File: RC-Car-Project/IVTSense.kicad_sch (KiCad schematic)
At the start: 12 parts, among them U7 INA229AQDGSRQ1, U8 ADC082S021CIMM/NOPB

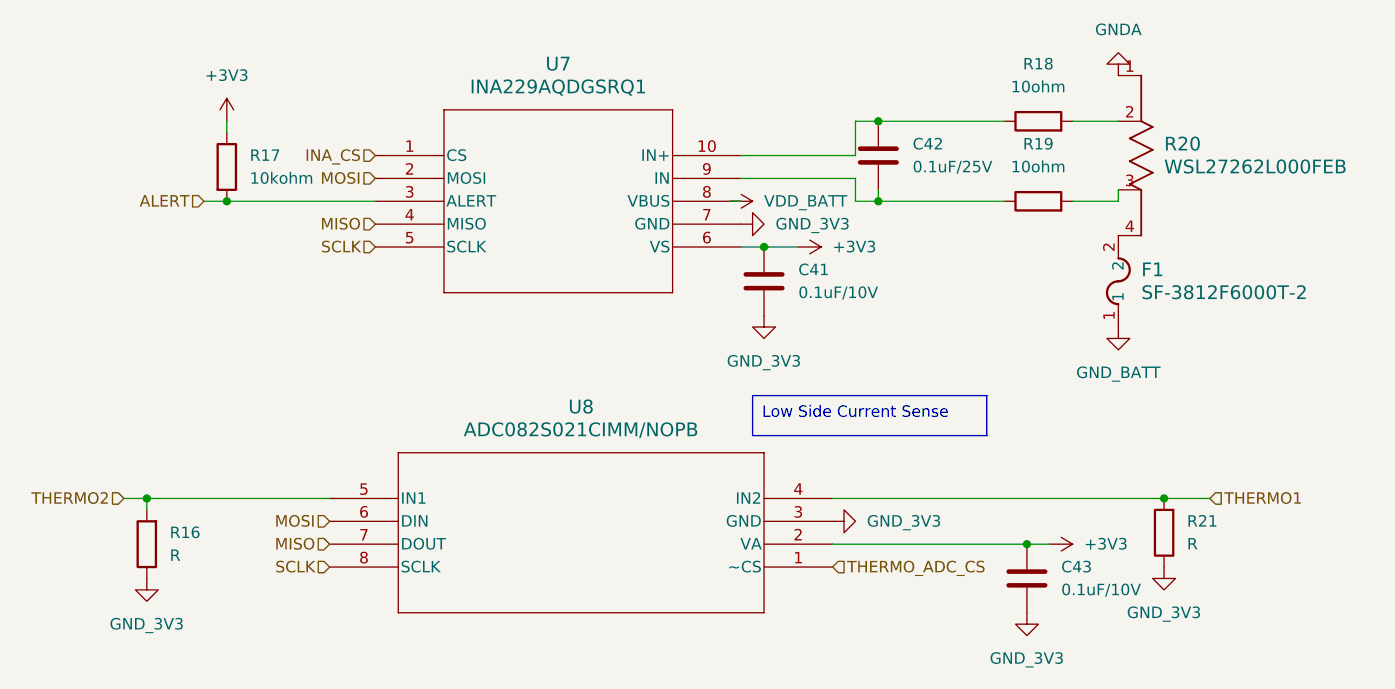
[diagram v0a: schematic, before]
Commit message: change footprint of cap some part num added
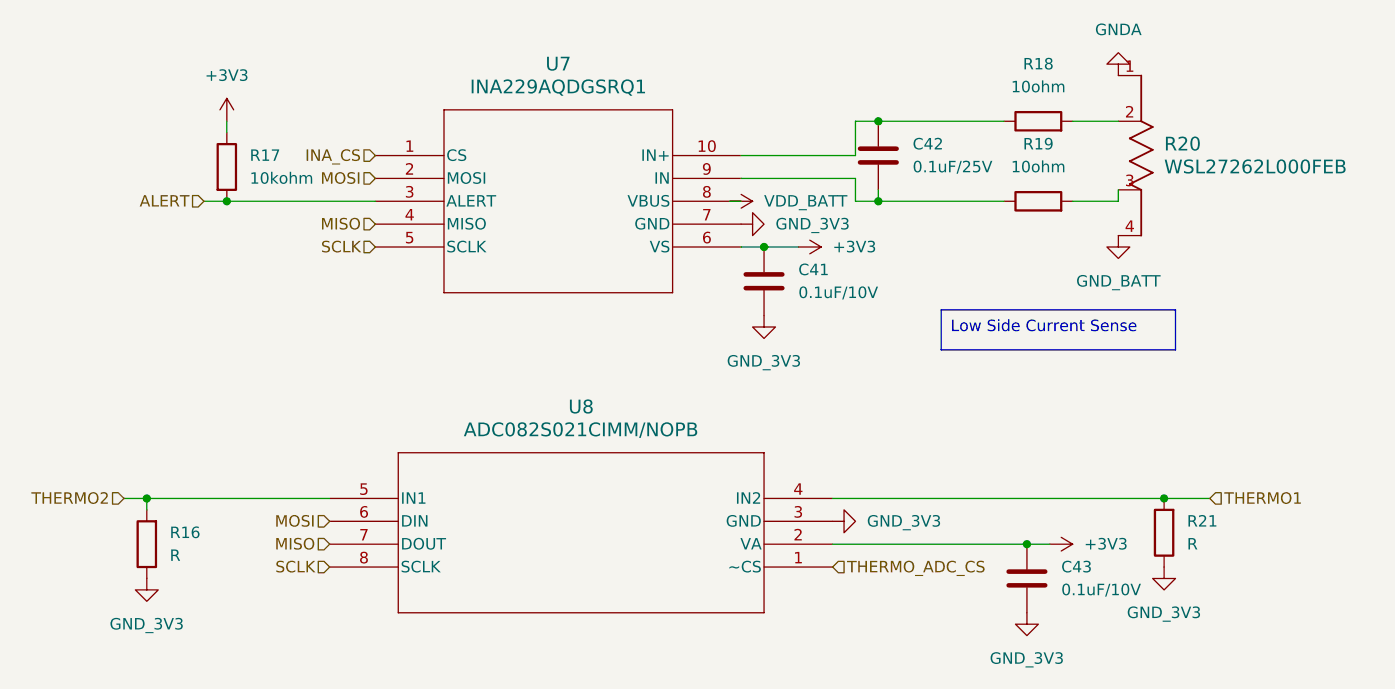
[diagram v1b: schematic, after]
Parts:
- removed F1: SF-3812F6000T-2, FUS_SF-3812F_BRN, symbol SF-3812F6000T-2:SF-3812F6000T-2
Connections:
- net GND_BATT: now also R20.4
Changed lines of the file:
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@@
 	(text_box "Low Side Current Sense\n"
 		(exclude_from_sim no)
-		(at 154.94 113.03 0)
+		(at 175.895 103.505 0)
 		(size 26.035 4.445)
 		(stroke
@@
 	)
 	(symbol
-		(lib_id "SF-3812F6000T-2:SF-3812F6000T-2")
-		(at 195.58 105.41 90)
-		(unit 1)
-		(exclude_from_sim no)
-		(in_bom yes)
-		(on_board yes)
-		(dnp no)
-		(fields_autoplaced yes)
-		(property "Reference" "F1"
-			(at 198.12 99.0599 90)
-			(effects
-				(font
-					(size 1.524 1.524)
-				)
-				(justify right)
-			)
-		)
-		(property "Value" "SF-3812F6000T-2"
-			(at 198.12 101.5999 90)
-			(effects
-				(font
-					(size 1.524 1.524)
-				)
-				(justify right)
-			)
-		)
-		(property "Footprint" "FUS_SF-3812F_BRN"
-			(at 195.58 105.41 0)
-			(effects
-				(font
-					(size 1.27 1.27)
-					(italic yes)
-				)
-				(hide yes)
-			)
-		)
-		(property "Datasheet" "SF-3812F6000T-2"
-			(at 195.58 105.41 0)
-			(effects
-				(font
-					(size 1.27 1.27)
-					(italic yes)
-				)
-				(hide yes)
-			)
-		)
-		(property "Description" ""
-			(at 195.58 105.41 0)
-			(effects
-				(font
-					(size 1.27 1.27)
-				)
-				(hide yes)
-			)
-		)
-		(pin "2"
-		)
-		(pin "1"
-		)
-		(instances
-			(project "RC-Car-Project"
-				(path "/ba870fd1-751d-4755-8e1a-1ea86ca9e2f6/9035ce50-cc35-47ce-85b3-06db8b07dac9"
-					(reference "F1")
-					(unit 1)
-				)
-			)
-		)
-	)
-	(symbol
 		(lib_id "Device:R")
 		(at 87.63 129.54 180)
@@
 			)
 		)
+		(property "MANUF_PN" ""
+			(at 87.63 129.54 0)
+			(effects
+				(font
+					(size 1.27 1.27)
+				)
+				(hide yes)
+			)
+		)
 		(pin "1"
 		)
@@
 			)
 		)
+		(property "MANUF_PN" ""
+			(at 195.58 80.01 0)
+			(effects
+				(font
+					(size 1.27 1.27)
+				)
+				(hide yes)
+			)
+		)
 		(pin "2"
 		)
@@
 			)
 		)
+		(property "MANUF_PN" ""
+			(at 186.69 91.44 0)
+			(effects
+				(font
+					(size 1.27 1.27)
+				)
+				(hide yes)
+			)
+		)
 		(pin "1"
 		)
@@
 			)
 		)
+		(property "MANUF_PN" ""
+			(at 185.42 133.35 0)
+			(effects
+				(font
+					(size 1.27 1.27)
+				)
+				(hide yes)
+			)
+		)
 		(pin "2"
 		)
@@
 			)
 		)
+		(property "MANUF_PN" ""
+			(at 200.66 128.27 0)
+			(effects
+				(font
+					(size 1.27 1.27)
+				)
+				(hide yes)
+			)
+		)
 		(pin "1"
 		)
@@
 			)
 		)
+		(property "MANUF_PN" ""
+			(at 168.91 86.36 0)
+			(effects
+				(font
+					(size 1.27 1.27)
+				)
+				(hide yes)
+			)
+		)
 		(pin "2"
 		)
@@
 	(symbol
 		(lib_id "power:GND")
-		(at 195.58 105.41 0)
+		(at 195.58 95.25 0)
 		(unit 1)
 		(exclude_from_sim no)
@@
 		(fields_autoplaced yes)
 		(property "Reference" "#PWR097"
-			(at 195.58 111.76 0)
+			(at 195.58 101.6 0)
 			(effects
 				(font
@@
 		)
 		(property "Value" "GND_BATT"
-			(at 195.58 110.49 0)
+			(at 195.58 100.33 0)
 			(effects
 				(font
@@
 		)
 		(property "Footprint" ""
-			(at 195.58 105.41 0)
+			(at 195.58 95.25 0)
 			(effects
 				(font
@@
 		)
 		(property "Datasheet" ""
-			(at 195.58 105.41 0)
+			(at 195.58 95.25 0)
 			(effects
 				(font
@@
 		)
 		(property "Description" "Power symbol creates a global label with name \"GND\" , ground"
-			(at 195.58 105.41 0)
+			(at 195.58 95.25 0)
 			(effects
 				(font
@@
 			)
 		)
+		(property "MANUF_PN" ""
+			(at 113.03 86.36 0)
+			(effects
+				(font
+					(size 1.27 1.27)
+				)
+				(hide yes)
+			)
+		)
 		(pin "9"
 		)
@@
 			)
 		)
+		(property "MANUF_PN" ""
+			(at 186.69 82.55 0)
+			(effects
+				(font
+					(size 1.27 1.27)
+				)
+				(hide yes)
+			)
+		)
 		(pin "1"
 		)
@@
 			)
 		)
+		(property "MANUF_PN" ""
+			(at 163.83 132.08 0)
+			(effects
+				(font
+					(size 1.27 1.27)
+				)
+				(hide yes)
+			)
+		)
 		(pin "2"
 		)
@@
 			)
 		)
+		(property "MANUF_PN" ""
+			(at 96.52 87.63 0)
+			(effects
+				(font
+					(size 1.27 1.27)
+				)
+				(hide yes)
+			)
+		)
 		(pin "1"
 		)
@@
 			(at 156.21 100.33 0)
 			(effects
+				(font
+					(size 1.27 1.27)
+				)
+				(hide yes)
+			)
+		)
+		(property "MANUF_PN" ""
+			(at 156.21 100.33 0)
+			(effects

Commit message: Re added my fuse
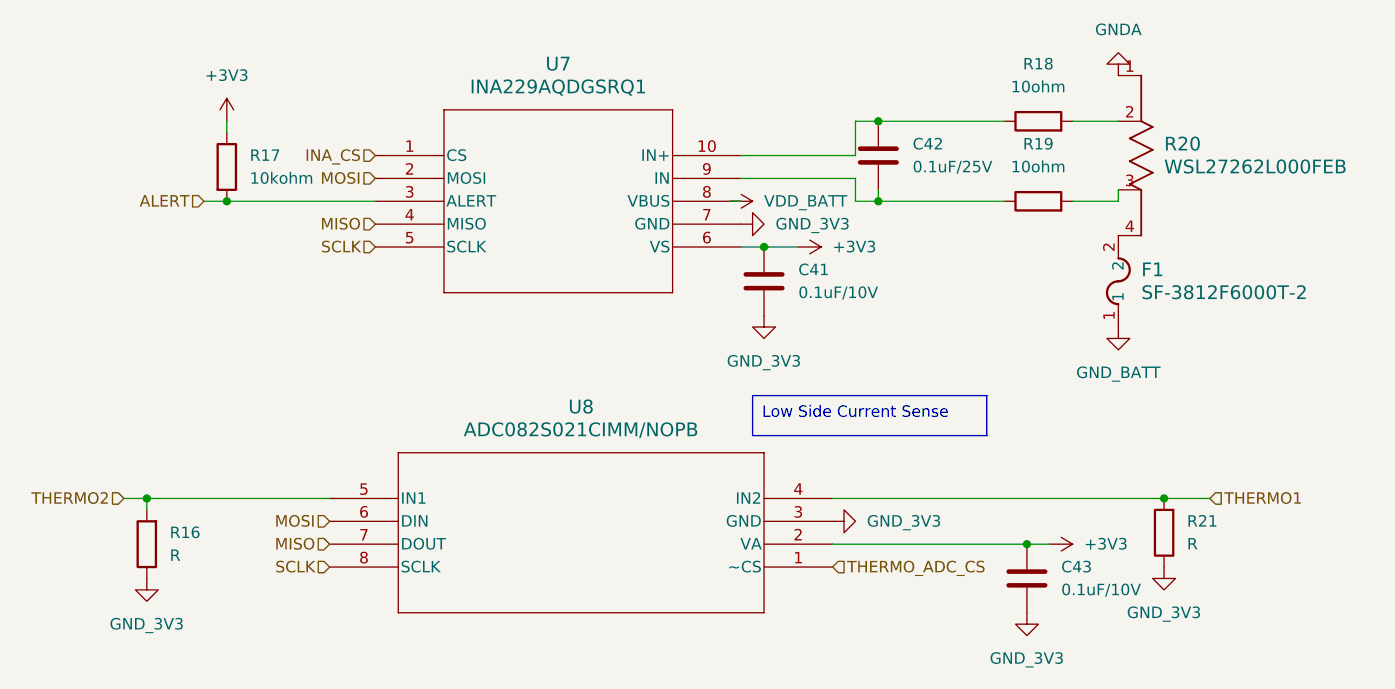
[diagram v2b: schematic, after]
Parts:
- added F1: SF-3812F6000T-2, FUS_SF-3812F_BRN, symbol SF-3812F6000T-2:SF-3812F6000T-2
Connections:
- net GND_BATT: now also F1.1; no longer R20.4
- new net: F1.2, R20.4
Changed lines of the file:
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@@
 	(text_box "Low Side Current Sense\n"
 		(exclude_from_sim no)
-		(at 175.895 103.505 0)
+		(at 154.94 113.03 0)
 		(size 26.035 4.445)
 		(stroke
@@
 	)
 	(symbol
+		(lib_id "SF-3812F6000T-2:SF-3812F6000T-2")
+		(at 195.58 105.41 90)
+		(unit 1)
+		(exclude_from_sim no)
+		(in_bom yes)
+		(on_board yes)
+		(dnp no)
+		(fields_autoplaced yes)
+		(property "Reference" "F1"
+			(at 198.12 99.0599 90)
+			(effects
+				(font
+					(size 1.524 1.524)
+				)
+				(justify right)
+			)
+		)
+		(property "Value" "SF-3812F6000T-2"
+			(at 198.12 101.5999 90)
+			(effects
+				(font
+					(size 1.524 1.524)
+				)
+				(justify right)
+			)
+		)
+		(property "Footprint" "FUS_SF-3812F_BRN"
+			(at 195.58 105.41 0)
+			(effects
+				(font
+					(size 1.27 1.27)
+					(italic yes)
+				)
+				(hide yes)
+			)
+		)
+		(property "Datasheet" "SF-3812F6000T-2"
+			(at 195.58 105.41 0)
+			(effects
+				(font
+					(size 1.27 1.27)
+					(italic yes)
+				)
+				(hide yes)
+			)
+		)
+		(property "Description" ""
+			(at 195.58 105.41 0)
+			(effects
+				(font
+					(size 1.27 1.27)
+				)
+				(hide yes)
+			)
+		)
+		(pin "2"
+		)
+		(pin "1"
+		)
+		(instances
+			(project ""
+				(path "/ba870fd1-751d-4755-8e1a-1ea86ca9e2f6/9035ce50-cc35-47ce-85b3-06db8b07dac9"
+					(reference "F1")
+					(unit 1)
+				)
+			)
+		)
+	)
+	(symbol
 		(lib_id "Device:C")
 		(at 168.91 86.36 0)
@@
 	(symbol
 		(lib_id "power:GND")
-		(at 195.58 95.25 0)
+		(at 195.58 105.41 0)
 		(unit 1)
 		(exclude_from_sim no)
@@
 		(fields_autoplaced yes)
 		(property "Reference" "#PWR097"
-			(at 195.58 101.6 0)
+			(at 195.58 111.76 0)
 			(effects
 				(font
@@
 		)
 		(property "Value" "GND_BATT"
-			(at 195.58 100.33 0)
+			(at 195.58 110.49 0)
 			(effects
 				(font
@@
 		)
 		(property "Footprint" ""
-			(at 195.58 95.25 0)
+			(at 195.58 105.41 0)
 			(effects
 				(font
@@
 		)
 		(property "Datasheet" ""
-			(at 195.58 95.25 0)
+			(at 195.58 105.41 0)
 			(effects
 				(font
@@
 		)
 		(property "Description" "Power symbol creates a global label with name \"GND\" , ground"
-			(at 195.58 95.25 0)
-			(effects
-				(font
+			(at 195.58 105.41 0)
+			(effects
+				(font

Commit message: Added Chip PNs
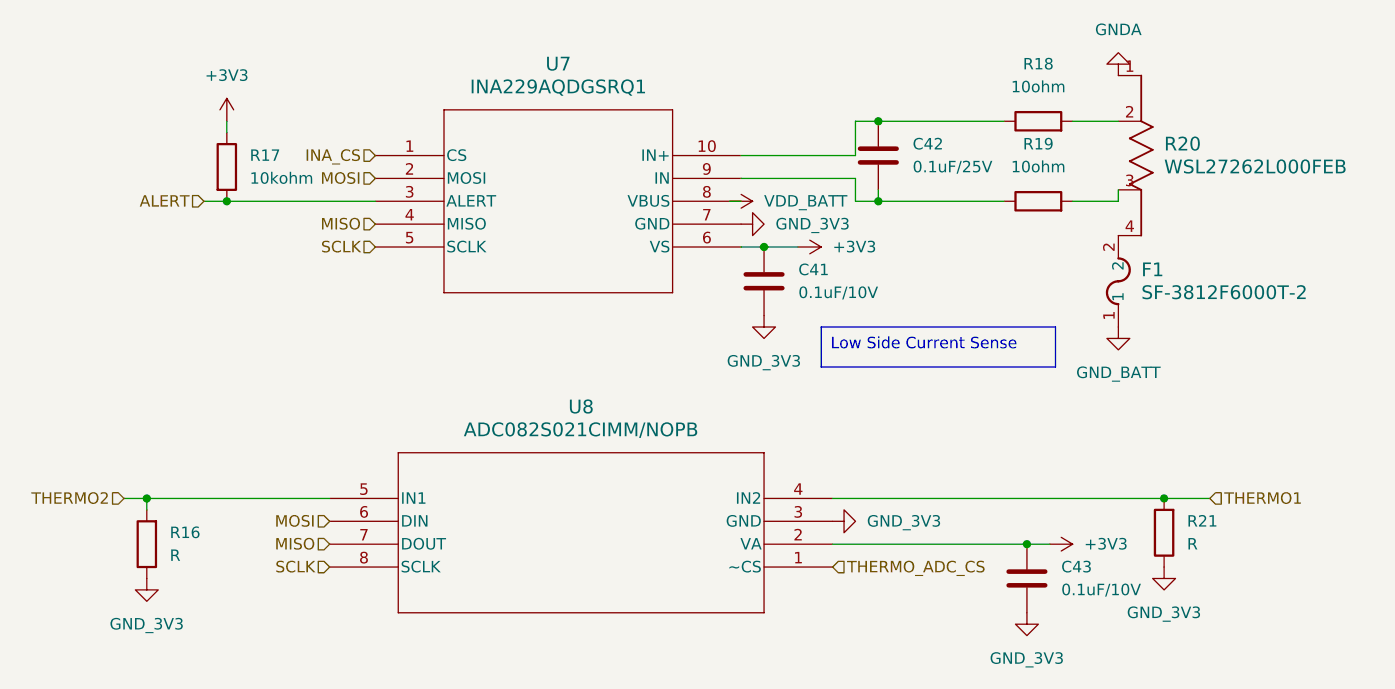
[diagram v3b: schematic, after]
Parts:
- U7: MANUF_PN (none) -> INA229AQDGSRQ1
- U8: MANUF_PN (none) -> ADC082S021CIMM/NOPB
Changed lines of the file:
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@@
 	(text_box "Low Side Current Sense\n"
 		(exclude_from_sim no)
-		(at 154.94 113.03 0)
+		(at 162.56 105.41 0)
 		(size 26.035 4.445)
 		(stroke
@@
 			)
 		)
-		(property "MANUF_PN" ""
+		(property "MANUF_PN" "INA229AQDGSRQ1"
 			(at 113.03 86.36 0)
 			(effects
@@
 			)
 		)
-		(property "Description" ""
+		(property "Description" "IC ADC 8BIT SAR 8VSSOP"
 			(at 163.83 132.08 0)
 			(effects
@@
 			)
 		)
-		(property "MANUF_PN" ""
+		(property "MANUF_PN" "ADC082S021CIMM/NOPB"
 			(at 163.83 132.08 0)
 			(effects

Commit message: Add caps
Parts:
- C41, C43: MANUF_PN (none) -> C0603C104K5RAC7411
- C42: value 0.1uF/25V -> 0.1uF/10V; MANUF_PN (none) -> C0603C104K5RAC7411
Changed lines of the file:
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@@
 			)
 		)
-		(property "MANUF_PN" ""
+		(property "MANUF_PN" "C0603C104K5RAC7411"
 			(at 185.42 133.35 0)
 			(effects
@@
 			)
 		)
-		(property "Value" "0.1uF/25V"
+		(property "Value" "0.1uF/10V"
 			(at 172.72 87.6299 0)
 			(effects
@@
 			)
 		)
-		(property "MANUF_PN" ""
+		(property "MANUF_PN" "C0603C104K5RAC7411"
 			(at 168.91 86.36 0)
 			(effects
@@
 			)
 		)
-		(property "MANUF_PN" ""
+		(property "MANUF_PN" "C0603C104K5RAC7411"
 			(at 156.21 100.33 0)
 			(effects
